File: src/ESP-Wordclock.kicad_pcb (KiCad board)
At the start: 2 copper layers, 235 x 235 mm, 308 parts, among them J101 Conn_01x08_Pin, J201 USB_C_Receptacle_USB2.0_16P, Q201 NPN BJT, Q202 NPN BJT, Q601 BSS138, SW301 SW_Push, SW302 SW_Push, U201 CP2102N-Axx-xQFN24, U301 ESP32-C3-WROOM-02, U302 TLV1117LV33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

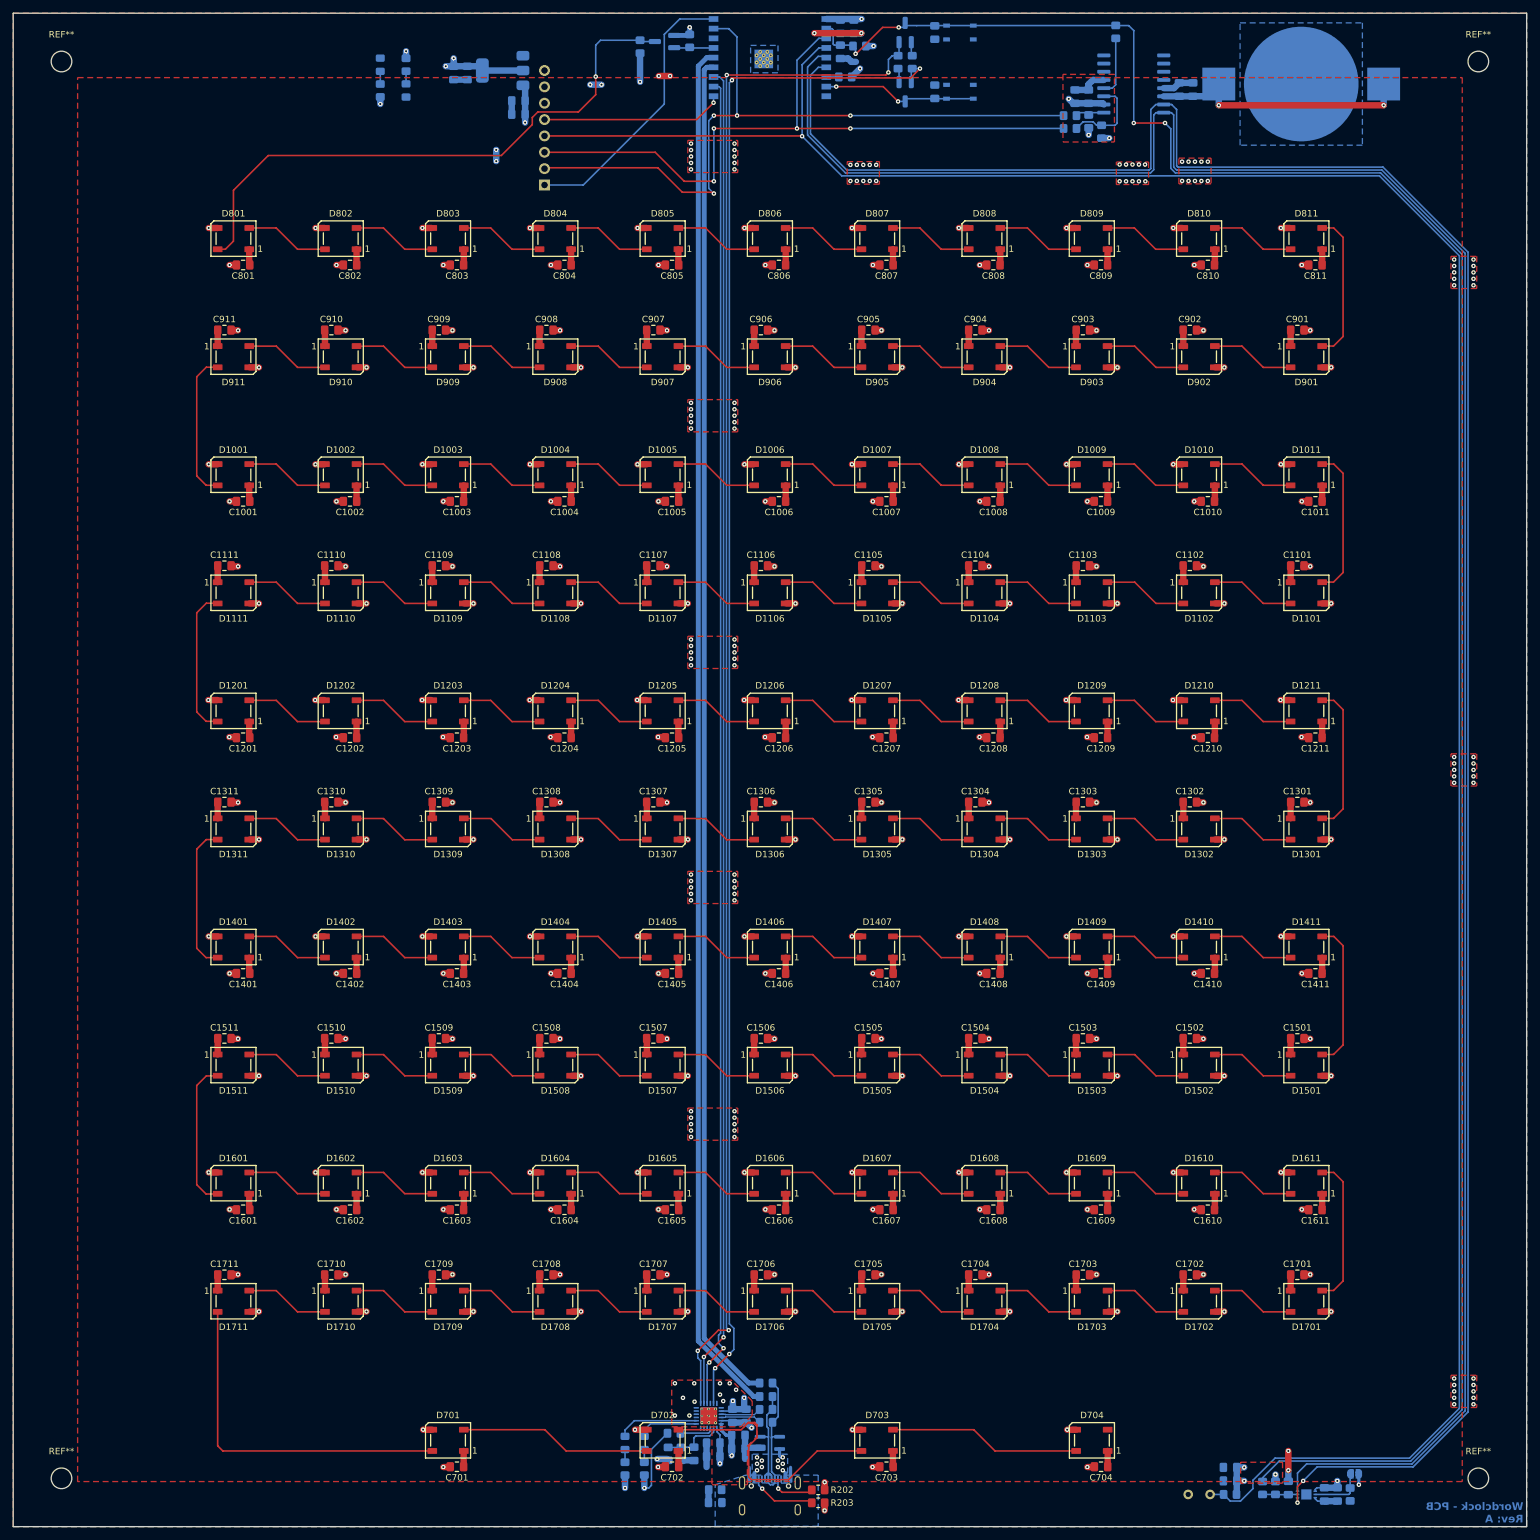
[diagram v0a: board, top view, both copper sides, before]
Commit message: Mod: Moved LEDs for the minutes 3 mm down and reexported all relevant files agian
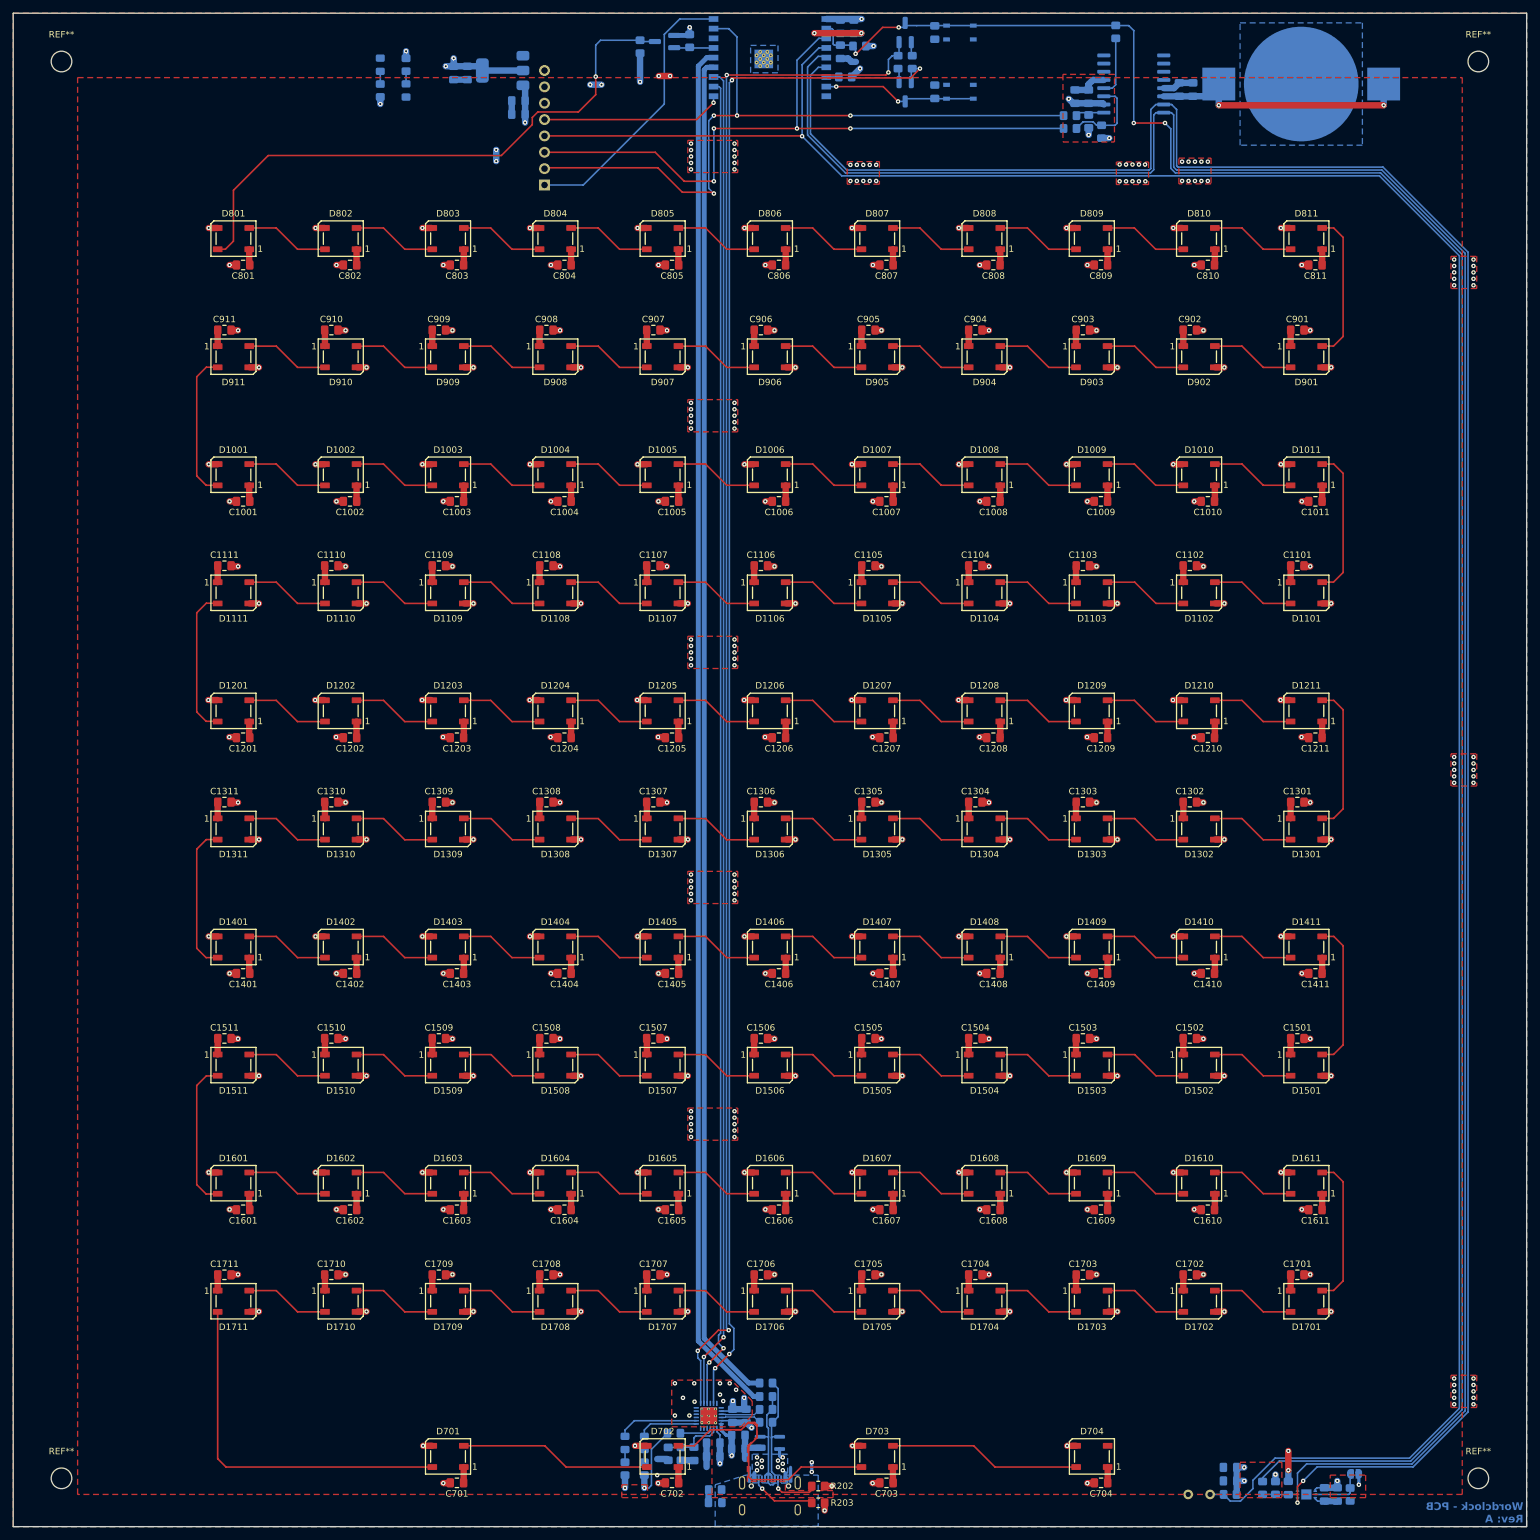
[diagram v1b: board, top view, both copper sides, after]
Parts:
- moved C701 2.50 mm to (103.9, 258.2)
- moved C702 2.50 mm to (137.3, 258.2)
- moved C703 2.50 mm to (170.6, 258.2)
- moved C704 2.50 mm to (203.9, 258.2)
- moved D701 2.50 mm to (102.5, 254.1)
- moved D702 2.50 mm to (135.8, 254.1)
- moved D703 2.50 mm to (169.2, 254.1)
- moved D704 2.50 mm to (202.5, 254.1)
- moved R202 0.60 mm to (160.0, 258.7)
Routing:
- net /LEDs/LED04-1/D_{IN}: track 54.5 -> 56.7 mm
- net +5V: track 304.3 -> 305.8 mm, vias 18 -> 20

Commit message: Add: JLCPCB Database and selected components for the assembly
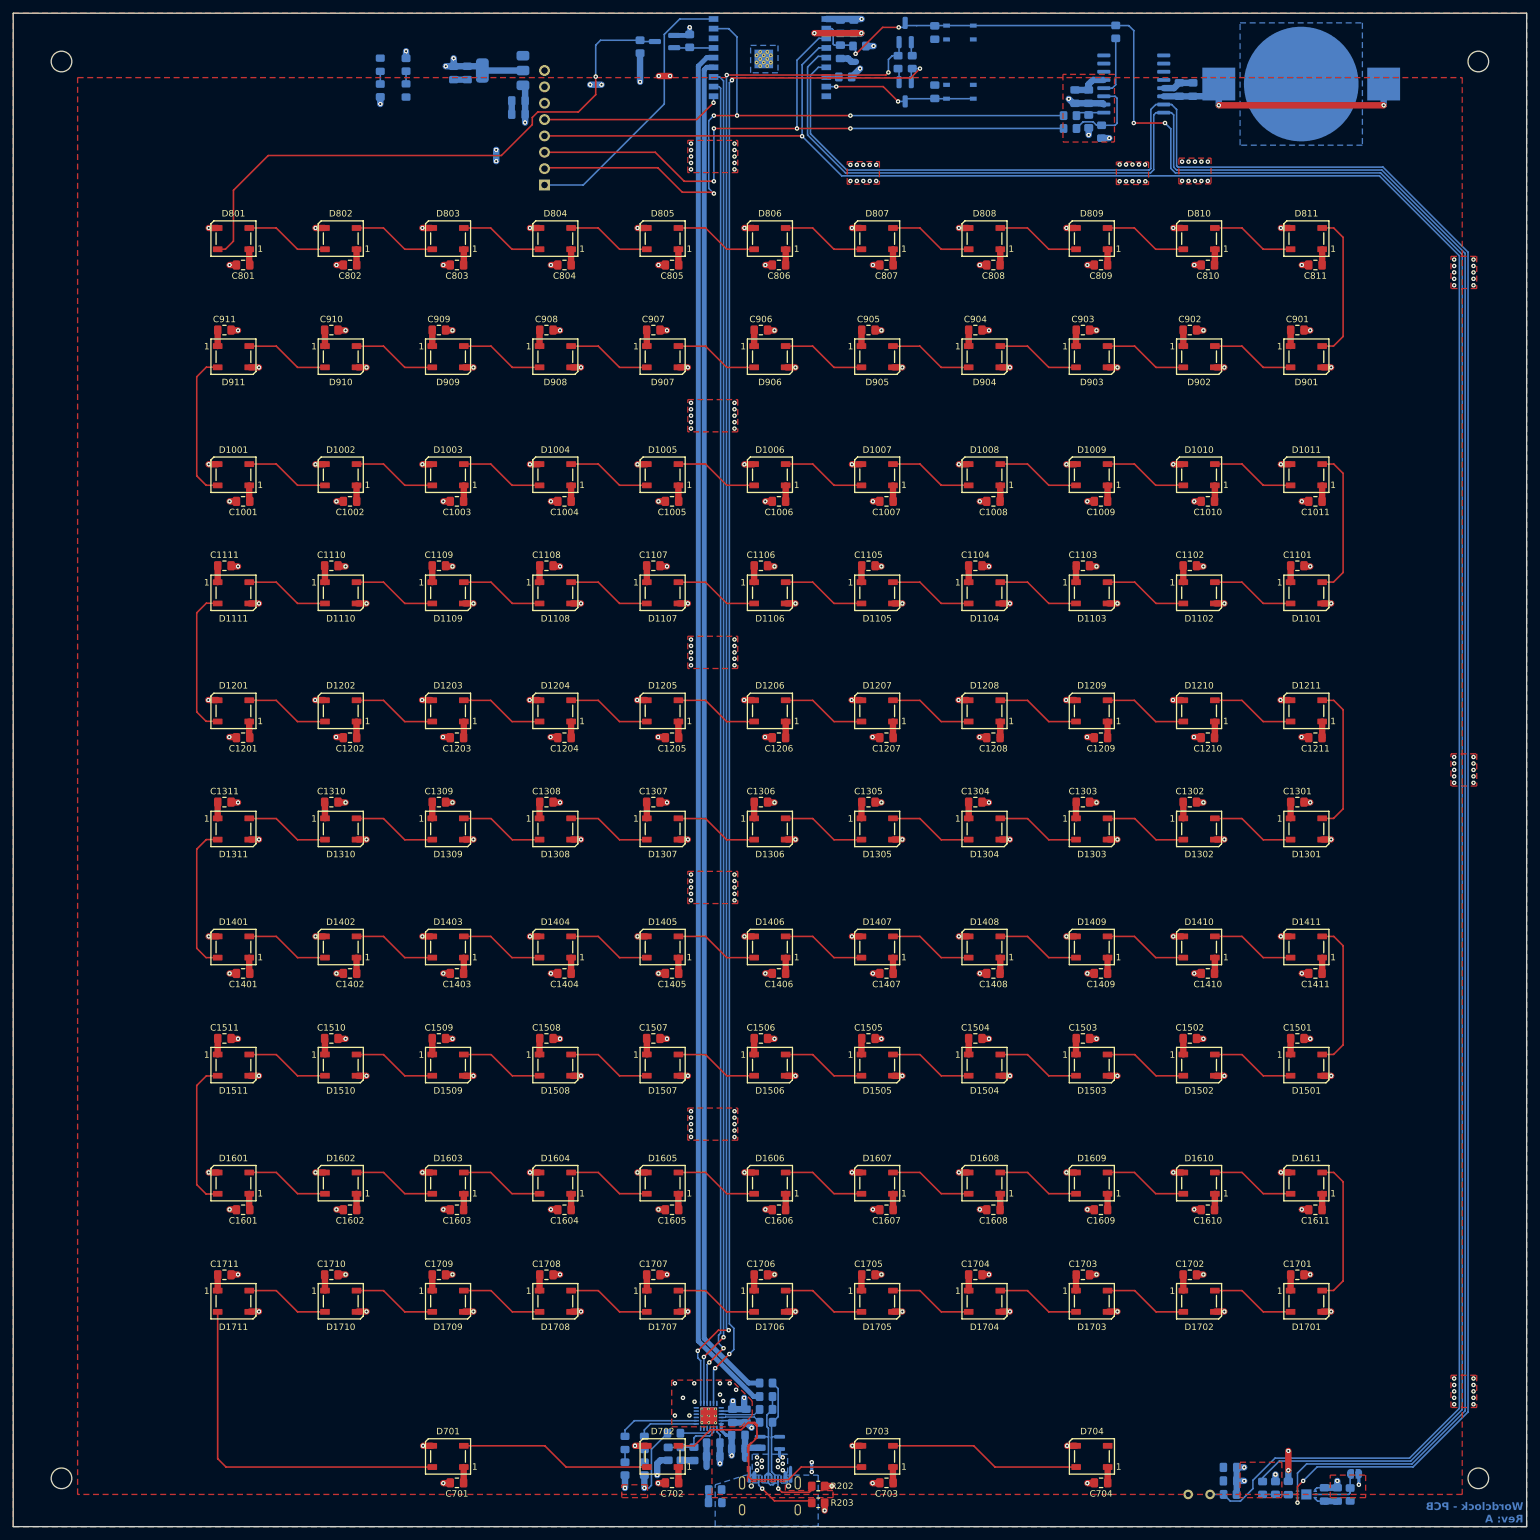
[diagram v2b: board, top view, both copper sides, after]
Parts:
- renumbered REF** to H1, REF** to H2, REF** to H3, REF** to H4
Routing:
- net +5V: track 305.8 -> 307.8 mm

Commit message: Add: JLCPCB order number placeholder
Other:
- board text added: "JLCJLCJLCJLC"
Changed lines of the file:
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@@
 	(title_block
 		(title "Wordclock - PCB")
-		(date "2024-11-05")
+		(date "2024-11-17")
 		(rev "A")
 		(company "ElektroNik Zoller")
@@
 		)
 	)
+	(gr_text "JLCJLCJLCJLC"
+		(at 37 263 -90)
+		(layer "B.SilkS")
+		(effects
+			(font
+				(size 1 1)
+				(thickness 0.15)
+			)
+			(justify left bottom mirror)
+		)
+	)
